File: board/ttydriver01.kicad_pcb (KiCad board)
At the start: 2 copper layers, 119.4 x 74.9 mm, 38 parts, among them P1 CONN_01X04, P2 CONN_01X02, P3 CONN_01X02, P4 CONN_01X10, Q1 IRLB8721PBF, T1 Coilcraft-DA2032, U1 NE555, U2 TPS2030P, U3 CP2102-breakout, U4 CPC1510G, U5 IE0524S, U6 CPC1510G

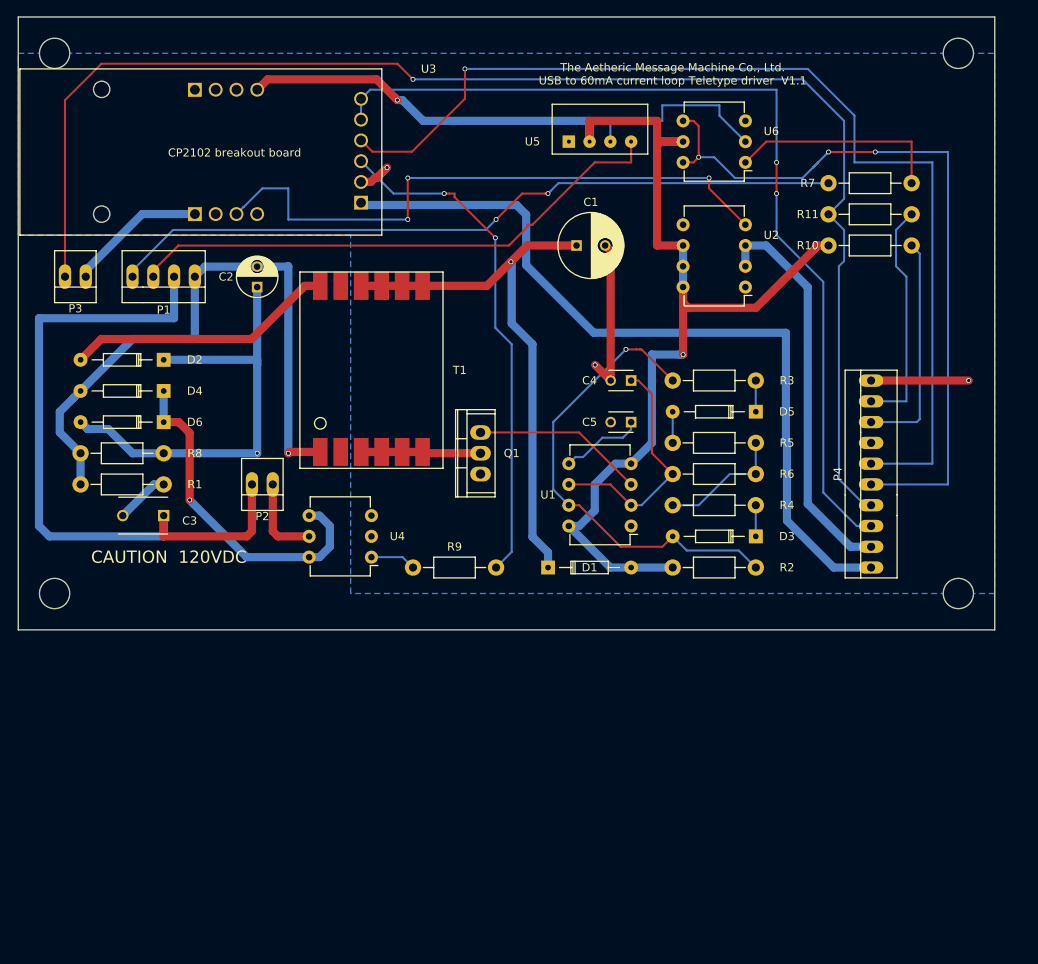
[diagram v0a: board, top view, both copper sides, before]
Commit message: Beginning board layout
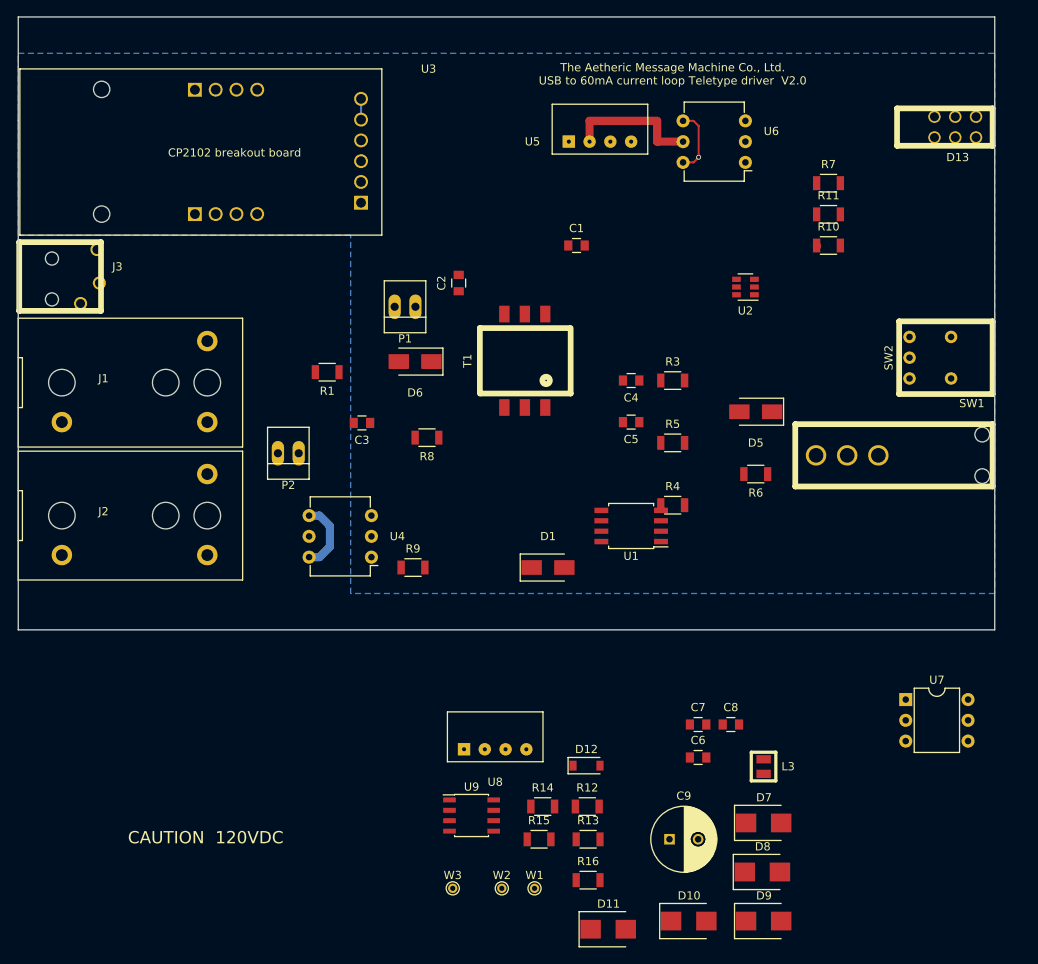
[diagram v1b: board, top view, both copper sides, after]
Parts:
- removed D2: D, Diodes_ThroughHole:Diode_DO-35_SOD27_Horizontal_RM10
- removed D3: 1N4148, Diodes_ThroughHole:Diode_DO-35_SOD27_Horizontal_RM10
- removed D4: ZENER 120V, Diodes_ThroughHole:Diode_DO-35_SOD27_Horizontal_RM10
- removed P3: CONN_01X02, Connect:PINHEAD1-2
- removed P4: CONN_01X10, DC-DC:PINHEAD1-10
- removed Q1: IRLB8721PBF, DC-DC:TO-220-HV
- removed R2: 4.7K, Resistors_ThroughHole:Resistor_Horizontal_RM10mm
- removed REF** (x4): MountingHole_3.7mm, Mounting_Holes:MountingHole_3.7mm
- added C6: 10nf, Capacitors_SMD:C_0805, F.Cu at (139.0, 168.0)
- added C7: 1000pf, Capacitors_SMD:C_0805, F.Cu at (139.0, 164.0)
- added C8: 880pf, Capacitors_SMD:C_0805, F.Cu at (143.0, 164.0)
- added C9: 1000uf, Capacitors_ThroughHole:C_Radial_D8_L11.5_P3.5, F.Cu at (135.5, 178.0)
- added D10: D_Zener, Diodes_SMD:SMB_Standard, F.Cu at (137.8, 188.0)
- added D11: D_Zener, Diodes_SMD:SMB_Standard, F.Cu at (128.0, 189.0)
- added D12: 4.7V Zener, Diodes_SMD:SOD-123, F.Cu at (125.3, 169.0)
- added D13: LED_3, Dialite:564-0100, F.Cu at (170.4, 90.9)
- added D7: D_Zener, Diodes_SMD:SMB_Standard, F.Cu at (147.0, 176.0)
- added D8: Schottky, Diodes_SMD:SMB_Standard, F.Cu at (146.8, 182.0)
- added D9: Schottky, Diodes_SMD:SMB_Standard, F.Cu at (147.0, 188.0)
- added J1: PRINTER JACK, Switchcraft:Switchcraft-SN37A12A, F.Cu at (61.2, 122.2)
- added J2: KEYBOARD JACK, Switchcraft:Switchcraft-SN37A12A, F.Cu at (61.2, 138.4)
- added J3: MOTOR CTL RELAY JACK, CUI:MJ-2509N, F.Cu at (56.0, 110.0)
- added L3: 10uH, Coilcraft:0508PS, F.Cu at (147.0, 169.1)
- added R12: 390, Resistors_SMD:R_1206, F.Cu at (125.5, 174.0)
- added R13: 3.3K, Resistors_SMD:R_1206, F.Cu at (125.5, 178.0)
- added R14: 1M, Resistors_SMD:R_1206, F.Cu at (120.0, 174.0)
- added R15: 680, Resistors_SMD:R_1206, F.Cu at (119.5, 178.0)
- added R16: 53.6K, Resistors_SMD:R_1206, F.Cu at (125.5, 183.0)
- added SW1: Switch_SPDT, NKK:Toggle-M2012SA2W40, F.Cu at (173.7, 131.1)
- added SW2: Button_SPDT, NKK:BB15AH-FA, F.Cu at (169.9, 119.1)
- added U7: CPC1510G, Housings_DIP:DIP-6_W7.62mm, F.Cu at (164.4, 160.9)
- added U8: IE0512S, DC-DC:IE0524S, F.Cu at (114.2, 167.0)
- added U9: FDS4559, Housings_SOIC:SOIC-8_3.9x4.9mm_Pitch1.27mm, F.Cu at (111.3, 175.1)
- added W1: TEST_1P, Connect:PINTST, F.Cu at (119.0, 184.0)
- added W2: TEST_1P, Connect:PINTST, F.Cu at (115.0, 184.0)
- added W3: TEST_1P, Connect:PINTST, F.Cu at (109.0, 184.0)
- C1: value 220uf -> 22uf; footprint Capacitors_ThroughHole:C_Radial_D8_L11.5_P3.5 -> Capacitors_SMD:C_0805
- C2: footprint Capacitors_ThroughHole:C_Radial_D5_L6_P2.5 -> Capacitors_SMD:C_0805
- C3: value 1000pf -> 10pf; footprint Capacitors_ThroughHole:C_Disc_D6_P5 -> Capacitors_SMD:C_0805
- C4: value 100pf -> 1000pf; footprint Capacitors_ThroughHole:C_Disc_D3_P2.5 -> Capacitors_SMD:C_0805
- C5: value 0.1uf -> 22uf; footprint Capacitors_ThroughHole:C_Disc_D3_P2.5 -> Capacitors_SMD:C_0805
- D1, D6: footprint Diodes_ThroughHole:Diode_DO-35_SOD27_Horizontal_RM10 -> Diodes_SMD:SMA_Standard
- D5: value 1N4148 -> D; footprint Diodes_ThroughHole:Diode_DO-35_SOD27_Horizontal_RM10 -> Diodes_SMD:SMA_Standard
- P1: value CONN_01X04 -> CONN_01X02; footprint DC-DC:PINHEAD1-4 -> Connect:PINHEAD1-2
- R1: footprint Resistors_ThroughHole:Resistor_Horizontal_RM10mm -> Resistors_SMD:R_1206
- R10, R11: value 680 -> 390; footprint Resistors_ThroughHole:Resistor_Horizontal_RM10mm -> Resistors_SMD:R_1206
- R3: value 4.7K -> 22; footprint Resistors_ThroughHole:Resistor_Horizontal_RM10mm -> Resistors_SMD:R_1206
- R4: value 22K -> 10K; footprint Resistors_ThroughHole:Resistor_Horizontal_RM10mm -> Resistors_SMD:R_1206
- R5: value 68K -> 27; footprint Resistors_ThroughHole:Resistor_Horizontal_RM10mm -> Resistors_SMD:R_1206
- R6: value 2.2K -> 720; footprint Resistors_ThroughHole:Resistor_Horizontal_RM10mm -> Resistors_SMD:R_1206
- R7: value 3.3K -> 7.2K; footprint Resistors_ThroughHole:Resistor_Horizontal_RM10mm -> Resistors_SMD:R_1206
- R8: value 1M -> 10K; footprint Resistors_ThroughHole:Resistor_Horizontal_RM10mm -> Resistors_SMD:R_1206
- R9: value 680 -> 33; footprint Resistors_ThroughHole:Resistor_Horizontal_RM10mm -> Resistors_SMD:R_1206
- T1: value Coilcraft-DA2032 -> Coilcraft-FA2469-AL; footprint Coilcraft:Coilcraft-DA2032-AL -> Coilcraft:Coilcraft-FA2469-AL
- U1: footprint Housings_DIP:DIP-8_W7.62mm -> Housings_SOIC:SOIJ-8_5.3x5.3mm_Pitch1.27mm
- U2: value TPS2030P -> AP2553W6; footprint Housings_DIP:DIP-8_W7.62mm -> TO_SOT_Packages_SMD:SOT-23-6
- moved R8 32.2 mm to (105.8, 128.9)
- moved D6 31.6 mm to (104.4, 119.6)
- moved P1 29.7 mm to (103.2, 112.9)
- moved C3 26.8 mm to (97.9, 127.1)
- moved C2 24.6 mm to (109.7, 110.0)
- moved R1 24.2 mm to (93.7, 120.9)
- moved T1 18.8 mm to (117.8, 119.5)
- moved P2 4.96 mm to (88.9, 130.8)
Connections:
- C1 pad 1: Net-(C1-Pad1) -> VCC
- C3 pad 1: /HVPOS -> Net-(C3-Pad1)
- C3 pad 2: Net-(C3-Pad2) -> GND
- D1 pad 1: Net-(C1-Pad1) -> Net-(C2-Pad1)
- D1 pad 2: VCC -> Net-(D1-Pad2)
- D5 pad 2: Net-(D5-Pad2) -> Net-(C2-Pad1)
- D6 pad 1: Net-(D4-Pad1) -> Net-(D5-Pad1)
- D6 pad 2: Net-(C2-Pad1) -> Net-(D6-Pad2)
- P1 pad 1: /HVNEG -> Net-(P1-Pad1)
- P1 pad 2: /HVPOS -> Net-(D6-Pad2)
- R1 pad 1: Net-(C3-Pad2) -> Net-(C7-Pad2)
- R10 pad 1: VCC -> Net-(D13-Pad6)
- R11 pad 2: Net-(P4-Pad9) -> Net-(J3-PadT)
- R3 pad 1: Net-(D3-Pad2) -> Net-(C3-Pad1)
- R3 pad 2: Net-(D5-Pad1) -> /OSC
- R4 pad 1: Net-(R4-Pad1) -> Net-(C3-Pad1)
- R4 pad 2: Net-(D3-Pad1) -> GND
- R5 pad 1: Net-(D5-Pad2) -> Net-(P1-Pad1)
- R5 pad 2: Net-(R4-Pad1) -> Net-(D12-Pad2)
- R6 pad 1: Net-(R4-Pad1) -> Net-(R6-Pad1)
- R6 pad 2: Net-(C4-Pad1) -> VCC
- R7 pad 1: Net-(P1-Pad4) -> Net-(R6-Pad1)
- R7 pad 2: Net-(R7-Pad2) -> Net-(C8-Pad1)
- R8 pad 1: Net-(C2-Pad1) -> Net-(D9-Pad2)
- R8 pad 2: /HVNEG -> /TxD
- R9 pad 1: Net-(R9-Pad1) -> Net-(D6-Pad2)
- R9 pad 2: /TxD -> Net-(P1-Pad1)
- T1 pad 1: /HVNEG -> Net-(C5-Pad1)
- T1 pad 3: Net-(Q1-Pad2) -> Net-(C4-Pad1)
- T1 pad 4: Net-(Q1-Pad2) -> /HVNEG
- T1 pad 5: Net-(Q1-Pad2) -> (no net)
- T1 pad 6: Net-(Q1-Pad2) -> Net-(D1-Pad2)
- U1 pad 2: Net-(C4-Pad1) -> Net-(D8-Pad1)
- U1 pad 5: Net-(C5-Pad1) -> Net-(C6-Pad1)
- U1 pad 6: Net-(C4-Pad1) -> Net-(C8-Pad1)
- U1 pad 7: Net-(D3-Pad2) -> Net-(R6-Pad1)
- U2 pad 1: GND -> Net-(SW1-Pad1)
- U2 pad 2: Net-(P4-Pad2) -> GND
- U2 pad 3: Net-(P4-Pad2) -> /ENABLE
- U2 pad 4: /ENABLE -> (no net)
- U3 pad 1-2: Net-(U3-Pad1-2) -> (no net)
- U3 pad 1-4: Net-(U3-Pad1-4) -> (no net)
- U3 pad 2-1: Net-(U3-Pad2-1) -> (no net)
- U3 pad 2-2: Net-(U3-Pad2-2) -> (no net)
- U3 pad 2-3: Net-(U3-Pad2-3) -> (no net)
- U3 pad 3-5: Net-(P4-Pad3) -> Net-(U3-Pad3-5)
- U3 pad 3-6: Net-(P4-Pad3) -> Net-(J3-PadT)
- U4 pad 1: Net-(R9-Pad1) -> Net-(R15-Pad1)
- U4 pad 3: Net-(U4-Pad3) -> (no net)
- U4 pad 4: Net-(D4-Pad1) -> Net-(D5-Pad1)
- U4 pad 6: Net-(D4-Pad1) -> Net-(D5-Pad1)
- U5 pad 4: Net-(P1-Pad3) -> Net-(J2-PadS)
- U6 pad 1: Net-(R7-Pad2) -> Net-(R13-Pad2)
- U6 pad 3: Net-(U6-Pad3) -> (no net)
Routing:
- net Net-(D13-Pad4): track 173.2 -> 0.00 mm, vias 1 -> 0
- net VCC: track 163.2 -> 16.5 mm, vias 2 -> 0
- net Net-(SW2-Pad3): track 129.1 -> 0.00 mm, vias 1 -> 0
- net Net-(P4-Pad3): track 113.0 -> 0.00 mm, vias 2 -> 0
- net Net-(SW1-Pad2): track 97.8 -> 0.40 mm
- net Net-(P1-Pad4): track 90.3 -> 0.00 mm, vias 2 -> 0
- net /HVPOS: track 84.6 -> 0.00 mm
- net /RxD: track 91.9 -> 8.15 mm, vias 3 -> 1
- net /HVNEG: track 76.8 -> 0.00 mm, vias 1 -> 0
- net /ENABLE: track 75.5 -> 0.00 mm, vias 3 -> 0
- net Net-(C1-Pad1): track 67.6 -> 0.00 mm, vias 1 -> 0
- net Net-(P1-Pad3): track 67.4 -> 0.00 mm
- net /TxD: track 62.7 -> 0.00 mm, vias 2 -> 0
- net Net-(D3-Pad2): track 57.9 -> 0.00 mm, vias 1 -> 0
- net Net-(C2-Pad1): track 55.6 -> 0.00 mm, vias 1 -> 0
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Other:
- board text added: "The Aetheric Message Machine Co., Ltd. USB to 60mA current loop Teletype driver V2.0"
- board text removed: "The Aetheric Message Machine Co., Ltd. USB to 60mA current loop Teletype driver V1.1"

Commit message: Minor board update
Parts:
- moved SW2 22.9 mm to (169.9, 96.3)
- moved D13 5.23 mm to (167.9, 86.4), turned to 180 degrees
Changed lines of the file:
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@@
   (general
     (links 109)
-    (no_connects 100)
+    (no_connects 102)
     (area 55.804999 77.394999 175.335001 152.475001)
     (thickness 1.6)
@@
     )
   )
-  (module Dialite:564-0100 (layer F.Cu)
-    (at 170.434 90.932)
-    (fp_text reference D13 (at 0.3 3.7) (layer F.SilkS)
-      (effects (font (size 1 1) (thickness 0.15)))
-    )
-    (fp_text value LED_3 (at 0 -3.81) (layer F.Fab)
-      (effects (font (size 1 1) (thickness 0.15)))
-    )
-    (fp_line (start 4.572 2.286) (end 4.572 -2.286) (layer F.SilkS) (width 0.7))
-    (fp_line (start -7.112 -2.286) (end -7.112 2.286) (layer F.SilkS) (width 0.7))
-    (fp_line (start -7.112 -2.286) (end 4.572 -2.286) (layer F.SilkS) (width 0.7))
-    (fp_line (start -7.112 2.286) (end 4.572 2.286) (layer F.SilkS) (width 0.7))
-    (pad 2 thru_hole circle (at -2.54 -1.27) (size 1.524 1.524) (drill 1.1) (layers *.Cu *.Mask)
-      (net 26 "Net-(D13-Pad2)"))
-    (pad 4 thru_hole circle (at 0 -1.27) (size 1.524 1.524) (drill 1.1) (layers *.Cu *.Mask)
-      (net 27 "Net-(D13-Pad4)"))
-    (pad 6 thru_hole circle (at 2.54 -1.27) (size 1.524 1.524) (drill 1.1) (layers *.Cu *.Mask)
-      (net 28 "Net-(D13-Pad6)"))
-    (pad 5 thru_hole circle (at 2.54 1.27) (size 1.524 1.524) (drill 1.1) (layers *.Cu *.Mask)
-      (net 25 "Net-(D12-Pad2)"))
-    (pad 3 thru_hole circle (at 0 1.27) (size 1.524 1.524) (drill 1.1) (layers *.Cu *.Mask)
-      (net 2 GND))
-    (pad 1 thru_hole circle (at -2.54 1.27) (size 1.524 1.524) (drill 1.1) (layers *.Cu *.Mask)
-      (net 2 GND))
-  )
   (module Switchcraft:Switchcraft-SN37A12A (layer F.Cu)
     (at 61.214 122.174 180)
@@
   )
   (module NKK:BB15AH-FA (layer F.Cu)
-    (at 169.926 119.126 90)
+    (at 169.926 96.266 90)
     (fp_text reference SW2 (at 0 -7.62 90) (layer F.SilkS)
       (effects (font (size 1 1) (thickness 0.15)))
@@
     )
   )
+  (module Dialite:564-0100 (layer F.Cu)
+    (at 167.894 86.36 180)
+    (fp_text reference D13 (at 0.3 3.7 180) (layer F.SilkS)
+      (effects (font (size 1 1) (thickness 0.15)))
+    )
+    (fp_text value LED_3 (at 0 -3.81 180) (layer F.Fab)
+      (effects (font (size 1 1) (thickness 0.15)))
+    )
+    (fp_line (start 4.572 2.286) (end 4.572 -2.286) (layer F.SilkS) (width 0.7))
+    (fp_line (start -7.112 -2.286) (end -7.112 2.286) (layer F.SilkS) (width 0.7))
+    (fp_line (start -7.112 -2.286) (end 4.572 -2.286) (layer F.SilkS) (width 0.7))
+    (fp_line (start -7.112 2.286) (end 4.572 2.286) (layer F.SilkS) (width 0.7))
+    (pad 2 thru_hole circle (at -2.54 -1.27 180) (size 1.524 1.524) (drill 1.1) (layers *.Cu *.Mask)
+      (net 26 "Net-(D13-Pad2)"))
+    (pad 4 thru_hole circle (at 0 -1.27 180) (size 1.524 1.524) (drill 1.1) (layers *.Cu *.Mask)
+      (net 27 "Net-(D13-Pad4)"))
+    (pad 6 thru_hole circle (at 2.54 -1.27 180) (size 1.524 1.524) (drill 1.1) (layers *.Cu *.Mask)
+      (net 28 "Net-(D13-Pad6)"))
+    (pad 5 thru_hole circle (at 2.54 1.27 180) (size 1.524 1.524) (drill 1.1) (layers *.Cu *.Mask)
+      (net 25 "Net-(D12-Pad2)"))
+    (pad 3 thru_hole circle (at 0 1.27 180) (size 1.524 1.524) (drill 1.1) (layers *.Cu *.Mask)
+      (net 2 GND))
+    (pad 1 thru_hole circle (at -2.54 1.27 180) (size 1.524 1.524) (drill 1.1) (layers *.Cu *.Mask)
+      (net 2 GND))
+    (model ${KIPRJMOD}/Dialite.3dshapes/564-100.wrl
+      (at (xyz 0 0 0))
+      (scale (xyz 1 1 1))
+      (rotate (xyz -90 0 90))
+    )
+  )

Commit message: Initial go at placement on board
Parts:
- removed P2: CONN_01X02, Connect:PINHEAD1-2
- added JP1: Jumper, Connect:PINHEAD1-2, F.Cu at (113.0, 117.6)
- D8, D9: footprint Diodes_SMD:SMB_Standard -> Diodes_SMD:SOD-323
- moved D10 95.9 mm to (81.0, 110.7)
- moved U7 92.2 mm to (106.4, 89.2)
- moved R12 90.6 mm to (170.7, 95.5), turned to 270 degrees
- moved D11 87.4 mm to (89.2, 110.7), turned to 180 degrees
- moved C9 75.0 mm to (152.1, 104.9)
- moved C7 70.4 mm to (87.4, 116.1)
- moved W2 63.6 mm to (157.7, 136.9)
- moved U8 61.8 mm to (128.8, 106.9)
- moved D12 57.0 mm to (124.2, 112.0), turned to 180 degrees
- moved D9 55.2 mm to (141.2, 133.1)
- moved L3 53.9 mm to (153.4, 115.6)
- moved R16 53.8 mm to (162.3, 143.8)
- moved D8 52.3 mm to (141.2, 130.0)
- moved R13 52.0 mm to (87.1, 143.0)
- moved W1 45.4 mm to (141.0, 144.3)
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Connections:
- P1 pad 2: Net-(D6-Pad2) -> /HVPOS
- R5 pad 1: Net-(P1-Pad1) -> Net-(JP1-Pad1)
- R9 pad 2: Net-(P1-Pad1) -> Net-(JP1-Pad1)
- U4 pad 5: Net-(P2-Pad1) -> Net-(P1-Pad1)
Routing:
- net VCC: track 16.5 -> 0.00 mm
- net /RxD: track 8.15 -> 0.00 mm, vias 1 -> 0

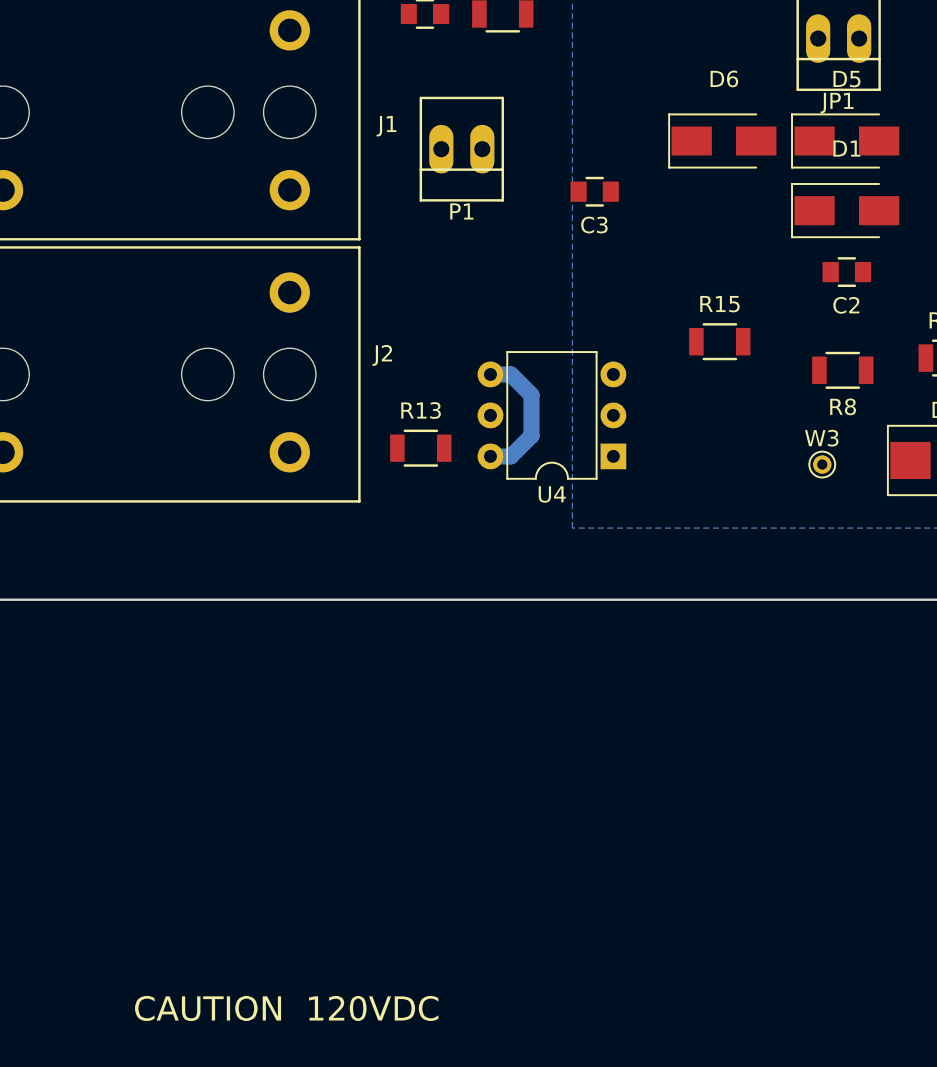
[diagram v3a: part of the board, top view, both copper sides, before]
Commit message: Fix minor placement problems
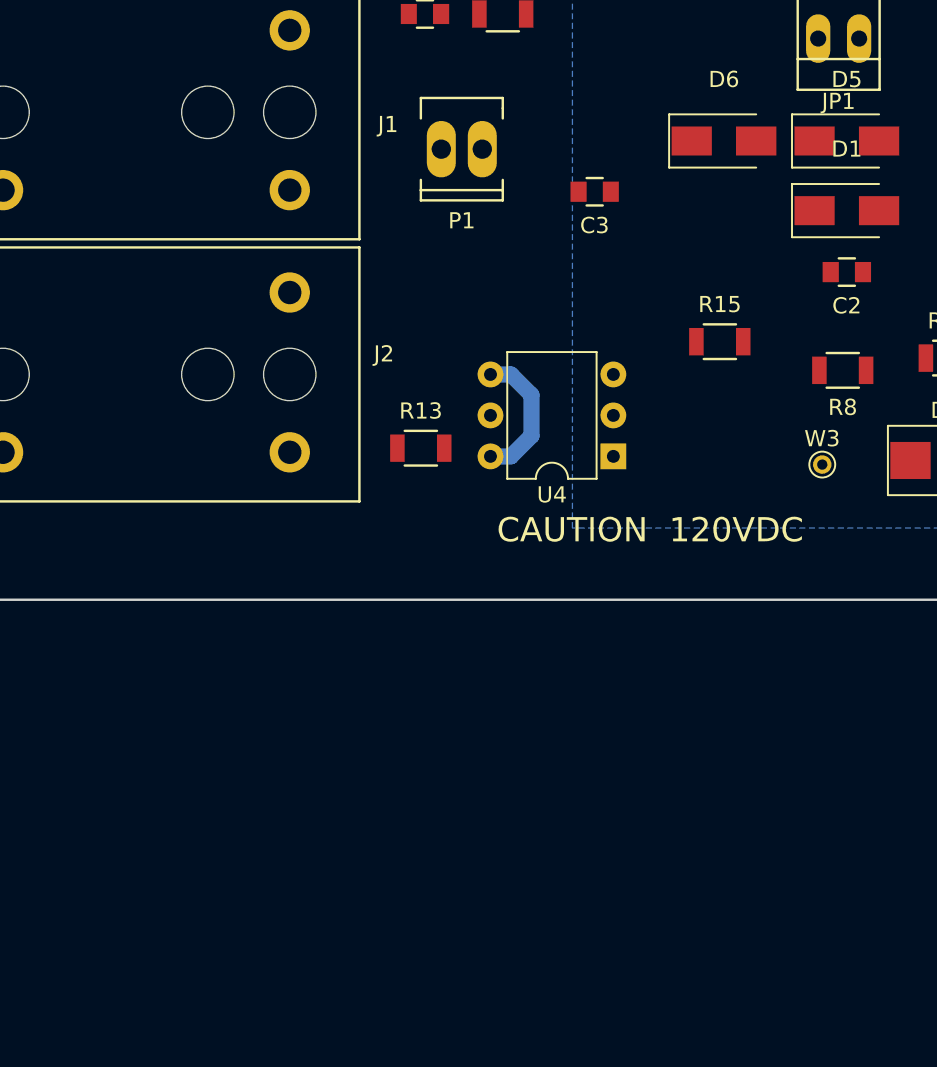
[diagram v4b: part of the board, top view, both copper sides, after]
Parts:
- P1: footprint Connect:PINHEAD1-2 -> Sockets_MOLEX_KK-System:Socket_MOLEX-KK-RM2-54mm_Lock_2pin_straight
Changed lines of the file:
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@@
     )
-  )
-  (module Connect:PINHEAD1-2 (layer F.Cu)
-    (at 89.662 124.46 180)
-    (attr virtual)
-    (fp_text reference P1 (at 0 -3.9 180) (layer F.SilkS)
-      (effects (font (size 1 1) (thickness 0.15)))
-    )
-    (fp_text value CONN_01X02 (at 0 3.81 180) (layer F.Fab)
-      (effects (font (size 1 1) (thickness 0.15)))
-    )
-    (fp_line (start 2.54 -1.27) (end -2.54 -1.27) (layer F.SilkS) (width 0.15))
-    (fp_line (start 2.54 3.175) (end -2.54 3.175) (layer F.SilkS) (width 0.15))
-    (fp_line (start -2.54 -3.175) (end 2.54 -3.175) (layer F.SilkS) (width 0.15))
-    (fp_line (start -2.54 -3.175) (end -2.54 3.175) (layer F.SilkS) (width 0.15))
-    (fp_line (start 2.54 -3.175) (end 2.54 3.175) (layer F.SilkS) (width 0.15))
-    (pad 1 thru_hole oval (at -1.27 0 180) (size 1.50622 3.01498) (drill 0.99822) (layers *.Cu *.Mask)
-      (net 31 "Net-(P1-Pad1)"))
-    (pad 2 thru_hole oval (at 1.27 0 180) (size 1.50622 3.01498) (drill 0.99822) (layers *.Cu *.Mask)
-      (net 11 /HVPOS))
   )
   (module Diodes_SMD:SMA_Standard (layer F.Cu)
@@
     )
   )
-  (gr_text "CAUTION  120VDC" (at 78.8 177.8) (layer F.SilkS)
+  (module Sockets_MOLEX_KK-System:Socket_MOLEX-KK-RM2-54mm_Lock_2pin_straight (layer F.Cu)
+    (at 89.662 124.46 180)
+    (descr "Socket, MOLEX, KK, RM 2.54mm, Lock, 2pin, straight,")
+    (tags "Socket, MOLEX, KK, RM 2.54mm, Lock, 2pin, straight,")
+    (fp_text reference P1 (at 0 -4.445 180) (layer F.SilkS)
+      (effects (font (size 1 1) (thickness 0.15)))
+    )
+    (fp_text value CONN_01X02 (at -0.635 5.08 180) (layer F.Fab)
+      (effects (font (size 1 1) (thickness 0.15)))
+    )
+    (fp_line (start -2.54 -2.54) (end 2.54 -2.54) (layer F.SilkS) (width 0.15))
+    (fp_line (start 2.54 3.175) (end 2.54 1.905) (layer F.SilkS) (width 0.15))
+    (fp_line (start 2.54 -2.54) (end 2.54 -1.905) (layer F.SilkS) (width 0.15))
+    (fp_line (start -2.54 2.54) (end -2.54 1.905) (layer F.SilkS) (width 0.15))
+    (fp_line (start -2.54 -2.54) (end -2.54 -1.905) (layer F.SilkS) (width 0.15))
+    (fp_line (start -2.54 -2.54) (end -2.54 -3.175) (layer F.SilkS) (width 0.15))
+    (fp_line (start -2.54 -3.175) (end 2.54 -3.175) (layer F.SilkS) (width 0.15))
+    (fp_line (start 2.54 -3.175) (end 2.54 -2.54) (layer F.SilkS) (width 0.15))
+    (fp_line (start 2.54 3.175) (end -2.54 3.175) (layer F.SilkS) (width 0.15))
+    (fp_line (start -2.54 3.175) (end -2.54 2.54) (layer F.SilkS) (width 0.15))
+    (pad 1 thru_hole oval (at -1.27 0 180) (size 1.80086 3.50012) (drill 1.19888) (layers *.Cu *.Mask)
+      (net 31 "Net-(P1-Pad1)"))
+    (pad 2 thru_hole oval (at 1.27 0 180) (size 1.80086 3.50012) (drill 1.19888) (layers *.Cu *.Mask)
+      (net 11 /HVPOS))
+  )
+  (gr_text "CAUTION  120VDC" (at 101.346 148.082) (layer F.SilkS)
     (effects (font (size 1.5 1.5) (thickness 0.3)))
   )
